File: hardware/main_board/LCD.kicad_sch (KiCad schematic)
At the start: 1 part, among them U2 HiLetGo_ST7735R

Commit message: drew schematic
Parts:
- renumbered U2 to U1
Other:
- note added: "Hierarchical Labels"
- moved on the sheet: U1
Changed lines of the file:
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@@
 	(paper "A4")
 	(rectangle
-		(start 46.99 17.78)
-		(end 115.57 80.01)
+		(start 15.24 13.97)
+		(end 44.45 41.91)
 		(stroke
 			(width 0)
@@
 		)
 	)
+	(rectangle
+		(start 15.24 43.18)
+		(end 83.82 105.41)
+		(stroke
+			(width 0)
+			(type default)
+		)
+		(fill
+			(type none)
+		)
+	)
 	(text "LCD"
 		(exclude_from_sim no)
-		(at 49.276 20.066 0)
+		(at 17.78 45.466 0)
+		(effects
+			(font
+				(size 1.27 1.27)
+			)
+		)
+	)
+	(text "Hierarchical Labels"
+		(exclude_from_sim no)
+		(at 25.4 15.24 0)
 		(effects
 			(font
@@
 	)
 	(junction
-		(at 107.95 54.61)
+		(at 76.2 80.01)
 		(diameter 0)
 		(color 0 0 0 0)
 	)
 	(junction
-		(at 107.95 29.21)
+		(at 76.2 54.61)
 		(diameter 0)
 		(color 0 0 0 0)
@@
 	(wire
 		(pts
-			(xy 107.95 50.8) (xy 107.95 54.61)
+			(xy 76.2 76.2) (xy 76.2 80.01)
 		)
 		(stroke
@@
 	(wire
 		(pts
-			(xy 53.34 52.07) (xy 67.31 52.07)
+			(xy 21.59 77.47) (xy 35.56 77.47)
 		)
 		(stroke
@@
 	(wire
 		(pts
-			(xy 107.95 29.21) (xy 107.95 33.02)
+			(xy 76.2 54.61) (xy 76.2 58.42)
 		)
 		(stroke
@@
 	)
 	(label "SPI1.MOSI"
-		(at 67.31 44.45 180)
+		(at 35.56 69.85 180)
 		(effects
 			(font
@@
 	)
 	(label "LCD_DC"
-		(at 67.31 48.26 180)
+		(at 35.56 73.66 180)
 		(effects
 			(font
@@
 	)
 	(label "CS_{SD}"
-		(at 67.31 60.96 180)
+		(at 35.56 86.36 180)
 		(effects
 			(font
@@
 	)
 	(label "CS_{LCD}"
-		(at 67.31 36.83 180)
+		(at 35.56 62.23 180)
 		(effects
 			(font
@@
 	)
 	(label "SPI1.SCK"
-		(at 67.31 40.64 180)
+		(at 35.56 66.04 180)
 		(effects
 			(font
@@
 	)
 	(label "SPI1.MOSI"
-		(at 67.31 64.77 180)
+		(at 35.56 90.17 180)
 		(effects
 			(font
@@
 	)
 	(label "SPI1.MISO"
-		(at 67.31 68.58 180)
+		(at 35.56 93.98 180)
 		(effects
 			(font
@@
 	)
 	(label "SPI1.SCK"
-		(at 67.31 72.39 180)
+		(at 35.56 97.79 180)
 		(effects
 			(font
@@
 	(symbol
 		(lib_id "power:+3V3")
-		(at 53.34 52.07 0)
+		(at 21.59 77.47 0)
 		(unit 1)
 		(exclude_from_sim no)
@@
 		(dnp no)
 		(fields_autoplaced yes)
-		(property "Reference" "#PWR02"
-			(at 53.34 55.88 0)
+		(property "Reference" "#PWR014"
+			(at 21.59 81.28 0)
 			(effects
 				(font
@@
 		)
 		(property "Value" "+3V3"
-			(at 53.34 46.99 0)
+			(at 21.59 72.39 0)
 			(effects
 				(font
@@
 		)
 		(property "Footprint" ""
-			(at 53.34 52.07 0)
+			(at 21.59 77.47 0)
 			(effects
 				(font
@@
 		)
 		(property "Datasheet" ""
-			(at 53.34 52.07 0)
+			(at 21.59 77.47 0)
 			(effects
 				(font
@@
 		)
 		(property "Description" "Power symbol creates a global label with name \"+3V3\""
-			(at 53.34 52.07 0)
+			(at 21.59 77.47 0)
 			(effects
 				(font
@@
 			(project ""
 				(path "/5332464e-0c3a-49d2-8fb5-731d0e42ee15/f60196d5-a61c-416f-993a-faa1a0858c5e"
-					(reference "#PWR02")
+					(reference "#PWR014")
 					(unit 1)
 				)
@@
 	(symbol
 		(lib_id "power:+3V3")
-		(at 107.95 29.21 0)
+		(at 76.2 54.61 0)
 		(unit 1)
 		(exclude_from_sim no)
@@
 		(dnp no)
 		(fields_autoplaced yes)
-		(property "Reference" "#PWR03"
-			(at 107.95 33.02 0)
+		(property "Reference" "#PWR013"
+			(at 76.2 58.42 0)
 			(effects
 				(font
@@
 		)
 		(property "Value" "+3V3"
-			(at 107.95 24.13 0)
+			(at 76.2 49.53 0)
 			(effects
 				(font
@@
 		)
 		(property "Footprint" ""
-			(at 107.95 29.21 0)
+			(at 76.2 54.61 0)
 			(effects
 				(font
@@
 		)
 		(property "Datasheet" ""
-			(at 107.95 29.21 0)
+			(at 76.2 54.61 0)
 			(effects
 				(font
@@
 		)
 		(property "Description" "Power symbol creates a global label with name \"+3V3\""
-			(at 107.95 29.21 0)
+			(at 76.2 54.61 0)
 			(effects
 				(font
@@
 			(project "main_board"
 				(path "/5332464e-0c3a-49d2-8fb5-731d0e42ee15/f60196d5-a61c-416f-993a-faa1a0858c5e"
-					(reference "#PWR03")
+					(reference "#PWR013")
 					(unit 1)
 				)
@@
 	(symbol
 		(lib_id "ECE445L:HiLetGo_ST7735R")
-		(at 87.63 41.91 0)
+		(at 55.88 67.31 0)
 		(unit 1)
 		(exclude_from_sim no)
@@
 		(dnp no)
 		(fields_autoplaced yes)
-		(property "Reference" "U2"
-			(at 87.63 21.59 0)
+		(property "Reference" "U1"
+			(at 55.88 46.99 0)
 			(effects
 				(font
@@
 		)
 		(property "Value" "HiLetGo_ST7735R"
-			(at 87.63 24.13 0)
+			(at 55.88 49.53 0)
 			(effects
 				(font
@@
 		)
 		(property "Footprint" "445L:hiletgo_st7735r"
-			(at 82.55 19.05 0)
+			(at 50.8 44.45 0)
 			(effects
 				(font
@@
 		)
 		(property "Datasheet" "https://users.ece.utexas.edu/~valvano/mspm0/1-8-tft-display.pdf"
-			(at 86.36 22.86 0)
+			(at 54.61 48.26 0)
 			(effects
 				(font
@@
 		)
 		(property "Description" "http://hiletgo.com/ProductDetail/2157911.html"
-			(at 87.63 41.91 0)
+			(at 55.88 67.31 0)
 			(effects
 				(font
@@
 		)
 		(property "Distributor" "Amazon"
-			(at 87.63 20.32 0)
+			(at 55.88 45.72 0)
 			(effects
 				(font
@@
 		)
 		(property "Manufacturer" "HiLetGo"
-			(at 72.39 20.32 0)
+			(at 40.64 45.72 0)
 			(effects
 				(font
@@
 		)
 		(property "P/N" "https://www.amazon.com/s?k=hiletgo+ST7735R"
-			(at 86.36 25.4 0)
+			(at 54.61 50.8 0)
 			(effects
 				(font
@@
 		)
 		(property "LCSC Part #" ""
-			(at 87.63 41.91 0)
+			(at 55.88 67.31 0)
 			(effects
 				(font
@@
 		)
 		(property "Cost" "9.95"
-			(at 99.06 19.05 0)
+			(at 67.31 44.45 0)
 			(effects
 				(font
@@
 			(project "main_board"
 				(path "/5332464e-0c3a-49d2-8fb5-731d0e42ee15/f60196d5-a61c-416f-993a-faa1a0858c5e"
-					(reference "U2")
+					(reference "U1")
 					(unit 1)
 				)
@@
 	(symbol
 		(lib_id "power:GND")
-		(at 107.95 54.61 0)
+		(at 76.2 80.01 0)
 		(unit 1)
 		(exclude_from_sim no)
@@
 		(dnp no)
 		(fields_autoplaced yes)
-		(property "Reference" "#PWR04"
-			(at 107.95 60.96 0)
+		(property "Reference" "#PWR015"
+			(at 76.2 86.36 0)
 			(effects
 				(font
@@
 		)
 		(property "Value" "GND"
-			(at 107.95 59.69 0)
+			(at 76.2 85.09 0)
 			(effects
 				(font
@@
 		)
 		(property "Footprint" ""
-			(at 107.95 54.61 0)
+			(at 76.2 80.01 0)
 			(effects
 				(font
@@
 		)
 		(property "Datasheet" ""
-			(at 107.95 54.61 0)
+			(at 76.2 80.01 0)
 			(effects
 				(font
@@
 		)
 		(property "Description" "Power symbol creates a global label with name \"GND\" , ground"
-			(at 107.95 54.61 0)
+			(at 76.2 80.01 0)
 			(effects
 				(font
@@
 			(project ""
 				(path "/5332464e-0c3a-49d2-8fb5-731d0e42ee15/f60196d5-a61c-416f-993a-faa1a0858c5e"
-					(reference "#PWR04")
+					(reference "#PWR015")
 					(unit 1)
 				)

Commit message: save before nuke SPI ADC
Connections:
- net CS_{LCD} renamed CS_LCD
- net CS_{SD} renamed CS_SD
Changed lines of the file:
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@@
 		)
 	)
-	(label "CS_{SD}"
+	(label "CS_SD"
 		(at 35.56 86.36 180)
 		(effects
@@
 		)
 	)
-	(label "CS_{LCD}"
+	(label "CS_LCD"
 		(at 35.56 62.23 180)
 		(effects
@@
 		)
 	)
-	(label "CS_{SD}"
+	(label "CS_SD"
 		(at 29.21 31.75 0)
 		(effects
@@
 		)
 	)
-	(label "CS_{LCD}"
+	(label "CS_LCD"
 		(at 29.21 34.29 0)
 		(effects
@@
 		)
 	)
-	(hierarchical_label "CS_{SD}"
+	(hierarchical_label "CS_SD"
 		(shape input)
 		(at 27.94 31.75 180)
@@
 		)
 	)
-	(hierarchical_label "CS_{LCD}"
+	(hierarchical_label "CS_LCD"
 		(shape input)
 		(at 27.94 34.29 180)

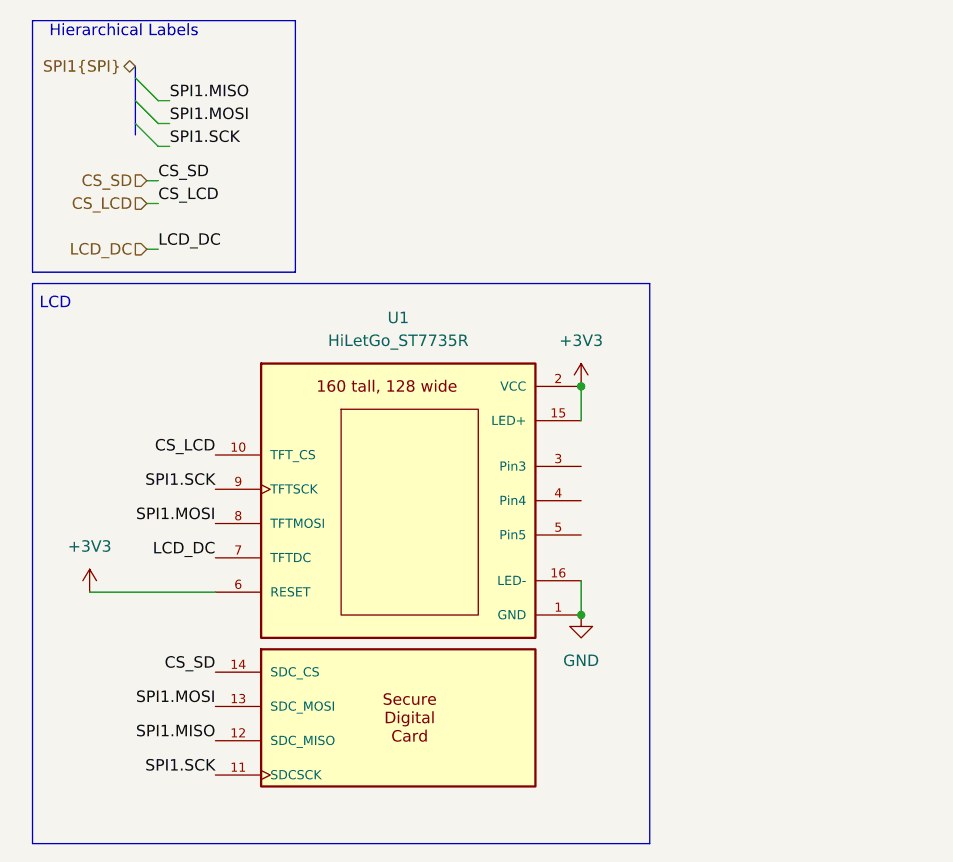
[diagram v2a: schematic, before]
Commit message: port to i2c for both boards. periph board passes drc
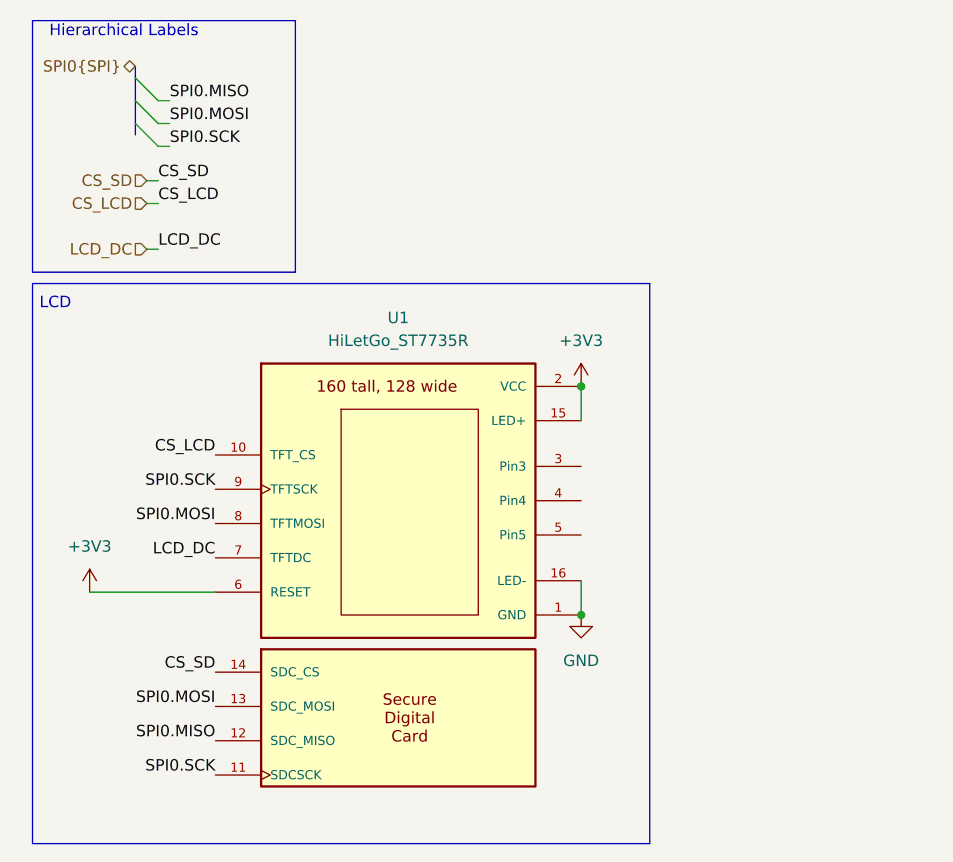
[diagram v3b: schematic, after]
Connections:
- net SPI1.MISO renamed SPI0.MISO
- net SPI1.MOSI renamed SPI0.MOSI
- net SPI1.SCK renamed SPI0.SCK
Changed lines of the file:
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@@
 		)
 	)
-	(label "SPI1.MOSI"
+	(label "SPI0.MOSI"
 		(at 35.56 69.85 180)
 		(effects
@@
 		)
 	)
-	(label "SPI1.SCK"
+	(label "SPI0.SCK"
 		(at 30.48 27.94 0)
 		(effects
@@
 		)
 	)
-	(label "SPI1.MISO"
+	(label "SPI0.MISO"
 		(at 30.48 22.86 0)
 		(effects
@@
 		)
 	)
-	(label "SPI1.SCK"
+	(label "SPI0.SCK"
 		(at 35.56 66.04 180)
 		(effects
@@
 		)
 	)
-	(label "SPI1.MOSI"
+	(label "SPI0.MOSI"
 		(at 35.56 90.17 180)
 		(effects
@@
 		)
 	)
-	(label "SPI1.MISO"
+	(label "SPI0.MISO"
 		(at 35.56 93.98 180)
 		(effects
@@
 		)
 	)
-	(label "SPI1.MOSI"
+	(label "SPI0.MOSI"
 		(at 30.48 25.4 0)
 		(effects
@@
 		)
 	)
-	(label "SPI1.SCK"
+	(label "SPI0.SCK"
 		(at 35.56 97.79 180)
 		(effects
@@
 		)
 	)
-	(hierarchical_label "SPI1{SPI}"
+	(hierarchical_label "SPI0{SPI}"
 		(shape bidirectional)
 		(at 26.67 19.05 180)
